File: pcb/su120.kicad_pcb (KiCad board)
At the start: 2 copper layers, 99.2 x 99.2 mm, 324 parts, among them J1 MJ-4PP-9, J2 Conn_01x03, J3 Conn_01x08, J4 Conn_01x08, J5 Conn_01x03, J6 MJ-4PP-9, SW1 SW_Push, SW10 SW_Push, SW11 SW_Push, SW12 SW_Push, SW13 SW_Push, SW14 SW_Push, SW15 SW_Push, SW16 SW_Push, SW17 SW_Push, SW18 SW_Push, SW19 SW_Push, SW2 SW_Push, SW20 SW_Push, SW3 SW_Push, SW4 SW_Push, SW5 SW_Push, SW6 SW_Push, SW7 SW_Push, SW8 SW_Push, SW9 SW_Push, U1 ProMicro

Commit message: Rev.3
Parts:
- removed the ? at (39.7, 69.1)
- removed the ? at (39.7, 59.4)
- removed the ? at (39.7, 73.8)
- removed the ? at (39.7, 64.7)
- removed the ? at (39.7, 93.5)
- removed the ? at (39.7, 98.8)
- removed the ? at (39.7, 109.9)
- removed the ? at (39.7, 114.5)
- removed the ? at (39.7, 103.2)
- removed the ? at (39.7, 119.9)
- removed the ? at (39.3, 145.7)
- removed the ? at (134.9, 59.5)
- removed the ? at (115.9, 59.5)
- removed the ? at (58.7, 78.6)
- removed the ? at (77.8, 78.6)
- removed the ? at (96.8, 78.6)
- removed the ? at (115.9, 78.6)
- removed the ? at (134.9, 78.6)
- removed the ? at (134.9, 97.6)
- removed the ? at (115.9, 97.6)
- removed the ? at (96.8, 97.6)
- removed the ? at (39.3, 150.4)
- removed the ? at (77.8, 97.6)
- removed the ? at (58.7, 97.6)
- removed the ? at (58.7, 116.7)
- removed the ? at (77.8, 116.7)
- removed the ? at (96.8, 116.7)
- removed the ? at (115.9, 116.7)
- removed the ? at (134.9, 116.7)
- removed the ? at (118.3, 135.7)
- removed the ? at (70.6, 135.7)
- removed the ? at (39.3, 134.9)
- removed the ? at (80.2, 54.8)
- removed the ? at (84.9, 54.8)
- removed the ? at (89.7, 54.8)
- removed the ? at (49.2, 54.8)
- removed the ? at (44.5, 54.8)
- removed the ? at (75.5, 54.8)
- removed the ? at (68.8, 54.8)
- removed the ? at (53.7, 54.8)
- removed the ? at (64.4, 54.8)
- removed the ? at (39.3, 141.7)
- removed the ? at (94.1, 54.8)
- removed the ? at (104.8, 54.8)
- removed the ? at (115.9, 54.8)
- removed the ? at (125.8, 54.8)
- removed the ? at (120.5, 54.8)
- removed the ? at (130.2, 54.8)
- removed the ? at (134.9, 54.8)
- removed the ? at (109.2, 54.8)
- removed the ? at (39.7, 54.8)
- removed the ? at (39.7, 78.3)
- removed the ? at (42.9, 136.4)
- removed the ? at (39.7, 88.9)
- removed the ? at (39.7, 124.2)
- removed the ? at (39.7, 131.0)
- removed the ? at (42.9, 150.4)
- removed the ? at (42.9, 141.7)
- removed the ? at (42.9, 145.7)
- removed the ? at (111.1, 142.9)
- removed H100, H101, H102, H103, H104, H105, H106, H107, H108, H109, H110, H111, H112, H141, H142, H143, H144, H145, H146, H147, H148, H149, H150, H151, H152, H49, H50, H51, H52, H53, H54, H55, H56, H57, H58, H59, H60, H61, H62, H63, H64, H65, H66, H67, H68, H69, H70, H71, H72, H73, H74, H75, H76, H77, H78, H79, H80, H81, H82, H83, H84, H85, H86, H87, H88, H89, H90, H91, H92, H93, H94, H95, H96, H97, H98, H99: MountingHole_Pad, #footprint:M2_Pad
- removed H153, H154, H155, H156, H158, H159, H160, H161, H162, H163, H164, H165, H166, H167, H168, H169, H170, H171, H172, H173, H174, H175, H176, H177, H178, H179, H180, H181, H182, H183, H184, H185, H186, H187, H188, H189, H190, H191, H192, H193, H194, H195, H196, H197, H198, H199, H200, H201, H202, H203, H204, H205, H206, H207, H208, H209: MountingHole_Pad, #footprint:M1.4_tapping_Pad
- added ?: , #footprint:M2, F.Cu at (99.2, 78.6)
- added ?: , #footprint:M1.4_tapping_Pad, F.Cu at (39.3, 142.1)
- added ?: , #footprint:M1.4_tapping_Pad, F.Cu at (39.3, 134.9)
- added ?: , #footprint:M1.4_tapping_Pad, F.Cu at (70.1, 55.2)
- added ?: , #footprint:M1.4_tapping_Pad, F.Cu at (82.9, 55.2)
- added ?: , #footprint:M1.4_tapping_Pad, F.Cu at (74.4, 55.2)
- added ?: , #footprint:M1.4_tapping_Pad, F.Cu at (40.1, 58.5)
- added ?: , #footprint:M1.4_tapping_Pad, F.Cu at (40.1, 67.1)
- added ?: , #footprint:M1.4_tapping_Pad, F.Cu at (44.5, 59.5)
- added ?: , #footprint:M1.4_tapping_Pad, F.Cu at (96.8, 59.5)
- added ?: , #footprint:M1.4_tapping_Pad, F.Cu at (101.6, 59.5)
- added ?: , #footprint:M2, F.Cu at (118.3, 73.8)
- added ?: , #footprint:M1.4_tapping_Pad, F.Cu at (115.9, 59.5)
- added ?: , #footprint:M1.4_tapping_Pad, F.Cu at (120.7, 59.5)
- added ?: , #footprint:M1.4_tapping_Pad, F.Cu at (134.9, 59.5)
- added ?: , #footprint:M1.4_tapping_Pad, F.Cu at (134.9, 73.8)
- added ?: , #footprint:M1.4_tapping_Pad, F.Cu at (120.7, 73.8)
- added ?: , #footprint:M1.4_tapping_Pad, F.Cu at (115.9, 73.8)
- added ?: , #footprint:M1.4_tapping_Pad, F.Cu at (101.6, 73.8)
- added ?: , #footprint:M1.4_tapping_Pad, F.Cu at (96.8, 73.8)
- added ?: , #footprint:M1.4_tapping_Pad, F.Cu at (44.5, 73.8)
- added ?: , #footprint:M1.4_tapping_Pad, F.Cu at (44.5, 78.6)
- added ?: , #footprint:M2, F.Cu at (115.9, 76.2)
- added ?: , #footprint:M1.4_tapping_Pad, F.Cu at (58.7, 78.6)
- added ?: , #footprint:M1.4_tapping_Pad, F.Cu at (63.5, 78.6)
- added ?: , #footprint:M1.4_tapping_Pad, F.Cu at (77.8, 78.6)
- added ?: , #footprint:M1.4_tapping_Pad, F.Cu at (82.5, 78.6)
- added ?: , #footprint:M1.4_tapping_Pad, F.Cu at (96.8, 78.6)
- added ?: , #footprint:M1.4_tapping_Pad, F.Cu at (101.6, 78.6)
- added ?: , #footprint:M1.4_tapping_Pad, F.Cu at (115.9, 78.6)
- added ?: , #footprint:M1.4_tapping_Pad, F.Cu at (120.7, 78.6)
- added ?: , #footprint:M1.4_tapping_Pad, F.Cu at (134.9, 78.6)
- added ?: , #footprint:M1.4_tapping_Pad, F.Cu at (134.9, 92.9)
- added ?: , #footprint:M2, F.Cu at (118.3, 78.6)
- added ?: , #footprint:M1.4_tapping_Pad, F.Cu at (120.7, 92.9)
- added ?: , #footprint:M1.4_tapping_Pad, F.Cu at (115.9, 92.9)
- added ?: , #footprint:M1.4_tapping_Pad, F.Cu at (101.6, 92.9)
- added ?: , #footprint:M1.4_tapping_Pad, F.Cu at (96.8, 92.9)
- added ?: , #footprint:M1.4_tapping_Pad, F.Cu at (82.5, 92.9)
- added ?: , #footprint:M1.4_tapping_Pad, F.Cu at (77.8, 92.9)
- added ?: , #footprint:M1.4_tapping_Pad, F.Cu at (63.5, 92.9)
- added ?: , #footprint:M1.4_tapping_Pad, F.Cu at (58.7, 92.9)
- added ?: , #footprint:M1.4_tapping_Pad, F.Cu at (44.5, 92.9)
- added ?: , #footprint:M1.4_tapping_Pad, F.Cu at (44.5, 97.6)
- added ?: , #footprint:M2, F.Cu at (120.7, 76.2)
- added ?: , #footprint:M1.4_tapping_Pad, F.Cu at (58.7, 97.6)
- added ?: , #footprint:M1.4_tapping_Pad, F.Cu at (63.5, 97.6)
- added ?: , #footprint:M1.4_tapping_Pad, F.Cu at (77.8, 97.6)
- added ?: , #footprint:M1.4_tapping_Pad, F.Cu at (82.5, 97.6)
- added ?: , #footprint:M1.4_tapping_Pad, F.Cu at (96.8, 97.6)
- added ?: , #footprint:M1.4_tapping_Pad, F.Cu at (101.6, 97.6)
- added ?: , #footprint:M1.4_tapping_Pad, F.Cu at (115.9, 97.6)
- added ?: , #footprint:M1.4_tapping_Pad, F.Cu at (120.7, 97.6)
- added ?: , #footprint:M1.4_tapping_Pad, F.Cu at (134.9, 97.6)
- added ?: , #footprint:M1.4_tapping_Pad, F.Cu at (134.9, 111.9)
- added ?: , #footprint:M2, F.Cu at (134.9, 76.2)
- added ?: , #footprint:M1.4_tapping_Pad, F.Cu at (120.7, 111.9)
- added ?: , #footprint:M1.4_tapping_Pad, F.Cu at (115.9, 111.9)
- added ?: , #footprint:M1.4_tapping_Pad, F.Cu at (101.6, 111.9)
- added ?: , #footprint:M1.4_tapping_Pad, F.Cu at (96.8, 111.9)
- added ?: , #footprint:M1.4_tapping_Pad, F.Cu at (82.5, 111.9)
- added ?: , #footprint:M1.4_tapping_Pad, F.Cu at (77.8, 111.9)
- added ?: , #footprint:M1.4_tapping_Pad, F.Cu at (63.5, 111.9)
- added ?: , #footprint:M1.4_tapping_Pad, F.Cu at (58.7, 111.9)
- added ?: , #footprint:M1.4_tapping_Pad, F.Cu at (44.5, 111.9)
- added ?: , #footprint:M1.4_tapping_Pad, F.Cu at (44.5, 116.7)
- added ?: , #footprint:M2, F.Cu at (134.9, 95.2)
- added ?: , #footprint:M1.4_tapping_Pad, F.Cu at (58.7, 116.7)
- added ?: , #footprint:M1.4_tapping_Pad, F.Cu at (63.5, 116.7)
- added ?: , #footprint:M1.4_tapping_Pad, F.Cu at (77.8, 116.7)
- added ?: , #footprint:M1.4_tapping_Pad, F.Cu at (82.5, 116.7)
- added ?: , #footprint:M1.4_tapping_Pad, F.Cu at (96.8, 116.7)
- added ?: , #footprint:M1.4_tapping_Pad, F.Cu at (101.6, 116.7)
- added ?: , #footprint:M1.4_tapping_Pad, F.Cu at (115.9, 116.7)
- added ?: , #footprint:M1.4_tapping_Pad, F.Cu at (120.7, 116.7)
- added ?: , #footprint:M1.4_tapping_Pad, F.Cu at (134.9, 116.7)
- added ?: , #footprint:M1.4_tapping_Pad, F.Cu at (134.9, 131.0)
- added ?: , #footprint:M2, F.Cu at (118.3, 92.9)
- added ?: , #footprint:M1.4_tapping_Pad, F.Cu at (120.7, 131.0)
- added ?: , #footprint:M1.4_tapping_Pad, F.Cu at (115.9, 131.0)
- added ?: , #footprint:M1.4_tapping_Pad, F.Cu at (101.6, 131.0)
- added ?: , #footprint:M1.4_tapping_Pad, F.Cu at (96.8, 131.0)
- added ?: , #footprint:M1.4_tapping_Pad, F.Cu at (82.5, 131.0)
- added ?: , #footprint:M1.4_tapping_Pad, F.Cu at (77.8, 131.0)
- added ?: , #footprint:M1.4_tapping_Pad, F.Cu at (63.5, 131.0)
- added ?: , #footprint:M1.4_tapping_Pad, F.Cu at (58.7, 131.0)
- added ?: , #footprint:M1.4_tapping_Pad, F.Cu at (44.5, 131.0)
- added ?: , #footprint:M1.4_tapping_Pad, F.Cu at (63.5, 135.7)
- added ?: , #footprint:M2, F.Cu at (120.7, 95.2)
- added ?: , #footprint:M1.4_tapping_Pad, F.Cu at (73.0, 135.7)
- added ?: , #footprint:M1.4_tapping_Pad, F.Cu at (87.3, 135.7)
- added ?: , #footprint:M1.4_tapping_Pad, F.Cu at (96.8, 135.7)
- added ?: , #footprint:M1.4_tapping_Pad, F.Cu at (101.6, 135.7)
- added ?: , #footprint:M1.4_tapping_Pad, F.Cu at (115.9, 135.7)
- added ?: , #footprint:M1.4_tapping_Pad, F.Cu at (120.7, 135.7)
- added ?: , #footprint:M1.4_tapping_Pad, F.Cu at (134.9, 135.7)
- added ?: , #footprint:M1.4_tapping_Pad, F.Cu at (134.9, 150.0)
- added ?: , #footprint:M1.4_tapping_Pad, F.Cu at (120.7, 150.0)
- added ?: , #footprint:M1.4_tapping_Pad, F.Cu at (115.9, 150.0)
- added ?: , #footprint:M2, F.Cu at (118.3, 97.6)
- added ?: , #footprint:M1.4_tapping_Pad, F.Cu at (101.6, 150.0)
- added ?: , #footprint:M1.4_tapping_Pad, F.Cu at (96.8, 150.0)
- added ?: , #footprint:M1.4_tapping_Pad, F.Cu at (87.3, 150.0)
- added ?: , #footprint:M1.4_tapping_Pad, F.Cu at (73.0, 150.0)
- added ?: , #footprint:M1.4_tapping_Pad, F.Cu at (63.5, 150.0)
- added ?: , #footprint:M1.4_tapping_Pad, F.Cu at (43.3, 142.1)
- added ?: , #footprint:M1.4_tapping_Pad, F.Cu at (43.3, 135.3)
- added ?: , #footprint:M1.4_tapping_Pad, F.Cu at (130.0, 55.2)
- added ?: , #footprint:M1.4_tapping_Pad, F.Cu at (135.3, 55.2)
- added ?: , #footprint:M1.4_tapping_Pad, F.Cu at (91.7, 55.2)
- added ?: , #footprint:M2, F.Cu at (134.9, 133.3)
- added ?: , #footprint:M2, F.Cu at (115.9, 95.2)
- added ?: , #footprint:M1.4_tapping_Pad, F.Cu at (86.4, 55.2)
- added ?: , #footprint:M1.4_tapping_Pad, F.Cu at (121.3, 55.2)
- added ?: , #footprint:M1.4_tapping_Pad, F.Cu at (112.5, 55.2)
- added ?: , #footprint:M1.4_tapping_Pad, F.Cu at (117.9, 55.2)
- added ?: , #footprint:M1.4_tapping_Pad, F.Cu at (126.6, 55.2)
- added ?: , #footprint:M1.4_tapping_Pad, F.Cu at (95.1, 55.2)
- added ?: , #footprint:M1.4_tapping_Pad, F.Cu at (100.4, 55.2)
- added ?: , #footprint:M1.4_tapping_Pad, F.Cu at (109.1, 55.2)
- added ?: , #footprint:M1.4_tapping_Pad, F.Cu at (103.8, 55.2)
- added ?: , #footprint:M1.4_tapping_Pad, F.Cu at (43.3, 150.4)
- added ?: , #footprint:M2, F.Cu at (99.2, 92.9)
- added ?: , #footprint:M1.4_tapping_Pad, F.Cu at (43.3, 145.7)
- added ?: , #footprint:M2, F.Cu at (101.6, 95.2)
- added ?: , #footprint:M2, F.Cu at (99.2, 97.6)
- added ?: , #footprint:M2, F.Cu at (96.8, 95.2)
- added ?: , #footprint:M2, F.Cu at (80.2, 92.9)
- added ?: , #footprint:M2, F.Cu at (82.5, 95.2)
- added ?: , #footprint:M2, F.Cu at (80.2, 97.6)
- added ?: , #footprint:M2, F.Cu at (77.8, 95.2)
- added ?: , #footprint:M2, F.Cu at (61.1, 92.9)
- added ?: , #footprint:M2, F.Cu at (80.2, 59.5)
- added ?: , #footprint:M2, F.Cu at (63.5, 95.2)
- added ?: , #footprint:M2, F.Cu at (61.1, 97.6)
- added ?: , #footprint:M2, F.Cu at (58.7, 95.2)
- added ?: , #footprint:M2, F.Cu at (44.5, 95.2)
- added ?: , #footprint:M2, F.Cu at (44.5, 114.3)
- added ?: , #footprint:M2, F.Cu at (58.7, 114.3)
- added ?: , #footprint:M2, F.Cu at (61.1, 111.9)
- added ?: , #footprint:M2, F.Cu at (63.5, 114.3)
- added ?: , #footprint:M2, F.Cu at (61.1, 116.7)
- added ?: , #footprint:M2, F.Cu at (77.8, 114.3)
- added ?: , #footprint:M2, F.Cu at (80.2, 73.8)
- added ?: , #footprint:M2, F.Cu at (80.2, 111.9)
- added ?: , #footprint:M2, F.Cu at (82.5, 114.3)
- added ?: , #footprint:M2, F.Cu at (80.2, 116.7)
- added ?: , #footprint:M2, F.Cu at (96.8, 114.3)
- added ?: , #footprint:M2, F.Cu at (99.2, 111.9)
- added ?: , #footprint:M2, F.Cu at (101.6, 114.3)
- added ?: , #footprint:M2, F.Cu at (99.2, 116.7)
- added ?: , #footprint:M2, F.Cu at (115.9, 114.3)
- added ?: , #footprint:M2, F.Cu at (118.3, 111.9)
- added ?: , #footprint:M2, F.Cu at (120.7, 114.3)
- added ?: , #footprint:M2, F.Cu at (115.9, 133.3)
- added ?: , #footprint:M2, F.Cu at (118.3, 116.7)
- added ?: , #footprint:M2, F.Cu at (134.9, 114.3)
- added ?: , #footprint:M2, F.Cu at (118.3, 150.0)
- added ?: , #footprint:M2, F.Cu at (120.7, 133.3)
- added ?: , #footprint:M2, F.Cu at (118.3, 135.7)
- added ?: , #footprint:M2, F.Cu at (118.3, 131.0)
- added ?: , #footprint:M2, F.Cu at (101.6, 133.3)
- added ?: , #footprint:M2, F.Cu at (96.8, 133.3)
- added ?: , #footprint:M2, F.Cu at (99.2, 150.0)
- added ?: , #footprint:M2, F.Cu at (99.2, 135.7)
- added ?: , #footprint:M2, F.Cu at (118.3, 59.5)
- added ?: , #footprint:M2, F.Cu at (99.2, 131.0)
- added ?: , #footprint:M2, F.Cu at (80.2, 131.0)
- added ?: , #footprint:M2, F.Cu at (61.1, 131.0)
- added ?: , #footprint:M1.4_tapping_Pad, F.Cu at (42.9, 55.2)
- added ?: , #footprint:M1.4_tapping_Pad, F.Cu at (52.4, 55.2)
- added ?: , #footprint:M1.4_tapping_Pad, F.Cu at (47.6, 55.2)
- added ?: , #footprint:M1.4_tapping_Pad, F.Cu at (59.1, 141.8)
- added ?: , #footprint:M1.4_tapping_Pad, F.Cu at (39.3, 145.7)
- added ?: , #footprint:M1.4_tapping_Pad, F.Cu at (39.3, 150.4)
- added ?: , #footprint:M1.4_tapping_Pad, F.Cu at (47.2, 150.4)
- added ?: , #footprint:M2, F.Cu at (61.1, 78.6)
- added ?: , #footprint:M1.4_tapping_Pad, F.Cu at (47.2, 142.1)
- added ?: , #footprint:M1.4_tapping_Pad, F.Cu at (47.2, 145.7)
- added ?: , #footprint:M1.4_tapping_Pad, F.Cu at (47.2, 135.3)
- added ?: , #footprint:M1.4_tapping_Pad, F.Cu at (51.2, 142.1)
- added ?: , #footprint:M1.4_tapping_Pad, F.Cu at (51.2, 145.7)
- added ?: , #footprint:M1.4_tapping_Pad, F.Cu at (51.2, 135.3)
- added ?: , #footprint:M1.4_tapping_Pad, F.Cu at (51.2, 150.4)
- added ?: , #footprint:M1.4_tapping_Pad, F.Cu at (55.2, 142.1)
- added ?: , #footprint:M1.4_tapping_Pad, F.Cu at (55.2, 145.7)
- added ?: , #footprint:M1.4_tapping_Pad, F.Cu at (55.2, 135.3)
- added ?: , #footprint:M2, F.Cu at (80.2, 78.6)
- added ?: , #footprint:M1.4_tapping_Pad, F.Cu at (55.2, 150.4)
- added ?: , #footprint:M1.4_tapping_Pad, F.Cu at (59.1, 135.4)
- added ?: , #footprint:M1.4_tapping_Pad, F.Cu at (59.1, 150.4)
- added ?: , #footprint:M1.4_tapping_Pad, F.Cu at (40.1, 80.2)
- added ?: , #footprint:M1.4_tapping_Pad, F.Cu at (40.1, 75.4)
- added ?: , #footprint:M1.4_tapping_Pad, F.Cu at (40.1, 84.9)
- added ?: , #footprint:M1.4_tapping_Pad, F.Cu at (40.1, 70.6)
- added ?: , #footprint:M1.4_tapping_Pad, F.Cu at (40.1, 88.5)
- added ?: , #footprint:M1.4_tapping_Pad, F.Cu at (40.1, 98.0)
- added ?: , #footprint:M1.4_tapping_Pad, F.Cu at (40.1, 102.8)
- added ?: , #footprint:M2, F.Cu at (101.6, 76.2)
- added ?: , #footprint:M1.4_tapping_Pad, F.Cu at (40.1, 93.3)
- added ?: , #footprint:M1.4_tapping_Pad, F.Cu at (56.0, 55.2)
- added ?: , #footprint:M1.4_tapping_Pad, F.Cu at (59.9, 55.2)
- added ?: , #footprint:M1.4_tapping_Pad, F.Cu at (66.7, 55.2)
- added ?: , #footprint:M1.4_tapping_Pad, F.Cu at (40.1, 106.4)
- added ?: , #footprint:M1.4_tapping_Pad, F.Cu at (40.1, 111.1)
- added ?: , #footprint:M1.4_tapping_Pad, F.Cu at (40.1, 120.7)
- added ?: , #footprint:M1.4_tapping_Pad, F.Cu at (40.1, 115.9)
- added ?: , #footprint:M1.4_tapping_Pad, F.Cu at (40.1, 131.4)
- added ?: , #footprint:M1.4_tapping_Pad, F.Cu at (40.1, 124.2)
- added D20: D, #footprint:diode_TH_SMD, F.Cu at (125.8, 134.9)
- added H210: MountingHole_Pad, #footprint:1pin_conn, F.Cu at (123.4, 134.9)
- added H211: MountingHole_Pad, #footprint:1pin_conn, F.Cu at (123.4, 150.8)
- added H212: MountingHole_Pad, #footprint:1pin_conn, F.Cu at (119.9, 143.3)
- added H213: MountingHole_Pad, #footprint:1pin_conn, F.Cu at (135.7, 143.3)
- added SW21: SW_Push, #footprint:CherryMX_MidHeight_Choc_Hotswap_rev4, F.Cu at (127.8, 142.9)
- SW1, SW10, SW11, SW12, SW13, SW14, SW15, SW16, SW17, SW19, SW2, SW20, SW3, SW4, SW5, SW6, SW7, SW8, SW9: footprint #footprint:CherryMX_MidHeight_Choc_Hotswap_rev2 -> #footprint:CherryMX_MidHeight_Choc_Hotswap_rev4
- moved ? 16.7 mm to (80.2, 142.9)
- moved D16 16.7 mm to (78.2, 134.9)
- moved H45 16.7 mm to (72.2, 143.3)
- moved H46 16.7 mm to (88.1, 143.3)
- moved SW16 16.7 mm to (80.2, 142.9)
- moved H41 16.7 mm to (75.8, 134.9)
- moved H43 16.7 mm to (75.8, 150.8)
- moved H42 2.38 mm to (104.4, 134.9)
- moved H44 2.38 mm to (104.4, 150.8)
- moved D17 2.38 mm to (106.8, 134.9)
- moved H47 2.38 mm to (100.8, 143.3)
- moved H48 2.38 mm to (116.7, 143.3)
- moved SW17 2.38 mm to (108.7, 142.9)
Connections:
- H41 pad 1: X1 -> X2
- H43 pad 1: X1 -> X2
- J1 pad A: Net-(J1-PadA) -> (no net)
- J6 pad A: Net-(J6-PadA) -> (no net)
- SW16 pad 1: X1 -> X2
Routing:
- net GND: track 1208.9 -> 978.4 mm, vias 52 -> 115
- net X2: track 87.2 -> 120.6 mm
- net X1: track 127.4 -> 95.9 mm
- net X5: track 153.9 -> 180.2 mm
- net Y5: track 252.8 -> 277.5 mm
- net Net-(D20-Pad2): track 0.00 -> 18.2 mm
- net X3: track 99.7 -> 101.5 mm
- net (no net): track 0.00 -> 1.68 mm
- net X4: track 160.0 -> 161.5 mm
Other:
- board size 99.2 x 99.2 mm -> 99.2 x 98.4 mm
- board text added: "0.25u"
- board text added: "0.5u"
- board text added: "0.75u"
- board text added: "1.25u"
- board text added: "1.5u"
- board text added: "1/8u"
- board text added: "1u"
- board text added: "2u"
- board text added: "3/8u"
- board text added: "5/8u"
- board text added: "SU120 Rev.3 by @e3w2q"
- board text added: "stagger"
- board text removed: "1/2"
- board text removed: "1/4"
- board text removed: "1/8"
- board text removed: "SU120 Rev.2 by @e3w2q"

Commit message: update
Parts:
- removed the ? at (99.2, 78.6)
- removed the ? at (118.3, 73.8)
- removed the ? at (115.9, 76.2)
- removed the ? at (118.3, 78.6)
- removed the ? at (120.7, 76.2)
- removed the ? at (134.9, 76.2)
- removed the ? at (134.9, 95.2)
- removed the ? at (118.3, 92.9)
- removed the ? at (120.7, 95.2)
- removed the ? at (118.3, 97.6)
- removed the ? at (134.9, 133.3)
- removed the ? at (115.9, 95.2)
- removed the ? at (99.2, 92.9)
- removed the ? at (101.6, 95.2)
- removed the ? at (99.2, 97.6)
- removed the ? at (96.8, 95.2)
- removed the ? at (80.2, 92.9)
- removed the ? at (82.5, 95.2)
- removed the ? at (80.2, 97.6)
- removed the ? at (77.8, 95.2)
- removed the ? at (61.1, 92.9)
- removed the ? at (63.5, 95.2)
- removed the ? at (61.1, 97.6)
- removed the ? at (58.7, 95.2)
- removed the ? at (44.5, 95.2)
- removed the ? at (44.5, 114.3)
- removed the ? at (58.7, 114.3)
- removed the ? at (61.1, 111.9)
- removed the ? at (63.5, 114.3)
- removed the ? at (61.1, 116.7)
- removed the ? at (77.8, 114.3)
- removed the ? at (80.2, 111.9)
- removed the ? at (82.5, 114.3)
- removed the ? at (80.2, 116.7)
- removed the ? at (96.8, 114.3)
- removed the ? at (99.2, 111.9)
- removed the ? at (101.6, 114.3)
- removed the ? at (99.2, 116.7)
- removed the ? at (115.9, 114.3)
- removed the ? at (118.3, 111.9)
- removed the ? at (120.7, 114.3)
- removed the ? at (115.9, 133.3)
- removed the ? at (118.3, 116.7)
- removed the ? at (134.9, 114.3)
- removed the ? at (118.3, 150.0)
- removed the ? at (120.7, 133.3)
- removed the ? at (118.3, 135.7)
- removed the ? at (118.3, 131.0)
- removed the ? at (101.6, 133.3)
- removed the ? at (96.8, 133.3)
- removed the ? at (99.2, 150.0)
- removed the ? at (99.2, 135.7)
- removed the ? at (118.3, 59.5)
- removed the ? at (99.2, 131.0)
- removed the ? at (80.2, 131.0)
- removed the ? at (61.1, 131.0)
- removed the ? at (61.1, 78.6)
- removed the ? at (80.2, 78.6)
- removed the ? at (101.6, 76.2)
- added ?: , #footprint:M2_spacer, F.Cu at (118.3, 76.2)
- added ?: , #footprint:M2_spacer, F.Cu at (118.3, 133.3)
- added ?: , #footprint:M2_spacer, F.Cu at (99.2, 133.3)
- added ?: , #footprint:M2_spacer, F.Cu at (118.3, 95.2)
- added ?: , #footprint:M2_spacer, F.Cu at (99.2, 95.2)
- added ?: , #footprint:M2_spacer, F.Cu at (80.2, 95.2)
- added ?: , #footprint:M2_spacer, F.Cu at (61.1, 95.2)
- added ?: , #footprint:M2_spacer, F.Cu at (61.1, 114.3)
- added ?: , #footprint:M2_spacer, F.Cu at (80.2, 114.3)
- added ?: , #footprint:M2_spacer, F.Cu at (99.2, 114.3)
- added ?: , #footprint:M2_spacer, F.Cu at (118.3, 114.3)
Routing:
- net (no net): track 1.68 -> 0.00 mm
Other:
- outline, holes or cut-outs redrawn

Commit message: Rev.4
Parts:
- removed the ? at (118.3, 133.3)
- removed the ? at (99.2, 133.3)
- removed the ? at (118.3, 95.2)
- removed the ? at (99.2, 95.2)
- removed the ? at (80.2, 95.2)
- removed the ? at (61.1, 95.2)
- removed the ? at (61.1, 114.3)
- removed the ? at (80.2, 114.3)
- removed the ? at (99.2, 114.3)
- removed the ? at (118.3, 114.3)
- removed H157: MountingHole_Pad, #footprint:M1.4_tapping_Pad
- added ?: , #footprint:M2_spacer, F.Cu at (99.2, 133.4)
- added ?: , #footprint:M2_spacer, F.Cu at (118.3, 95.3)
- added ?: , #footprint:M2_spacer, F.Cu at (118.3, 133.4)
- added ?: , #footprint:M2_spacer, F.Cu at (118.3, 114.3)
- added ?: , #footprint:M2_spacer, F.Cu at (99.2, 114.3)
- added ?: , #footprint:M2_spacer, F.Cu at (80.2, 114.3)
- added ?: , #footprint:M2_spacer, F.Cu at (61.1, 114.3)
- added ?: , #footprint:M2_spacer, F.Cu at (61.1, 95.3)
- added ?: , #footprint:M2_spacer, F.Cu at (80.2, 95.3)
- added ?: , #footprint:M2_spacer, F.Cu at (99.2, 95.3)
- J3, J4: footprint #footprint:PinHeader_1x08_P2.54mm_Vertical -> #footprint:PinHeader_1x08_P2.54mm_Vertical_rev2
- JP1, JP4, JP6: moved to F.Cu
- JP2, JP3, JP5: moved to B.Cu
- moved SW18 2.31 mm to (83.7, 64.4)
- moved JP2 1.26 mm to (46.8, 69.1)
- moved JP6 1.26 mm to (46.8, 69.1)
- moved JP1 1.26 mm to (46.8, 64.3)
- moved JP3 1.26 mm to (46.8, 64.3)
- moved JP4 1.19 mm to (46.8, 66.7)
- moved JP5 1.19 mm to (46.8, 66.7)
- moved J2 0.44 mm to (88.0, 72.0)
- moved J5 0.44 mm to (93.1, 72.0)
- moved ? 0.40 mm to (39.3, 142.5)
- moved ? 0.40 mm to (39.3, 135.3)
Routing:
- net GND: track 978.4 -> 988.5 mm, vias 115 -> 117
- net reset1: track 59.2 -> 55.2 mm, vias 5 -> 3
- net Y3: track 262.4 -> 264.7 mm
- net Y4: track 307.3 -> 309.6 mm
- net dummyVCC: track 53.4 -> 55.7 mm, vias 2 -> 1
- net X4: track 161.5 -> 163.1 mm
- net dummydata: track 53.2 -> 54.4 mm, vias 2 -> 1
- net reset2: track 41.3 -> 40.1 mm, vias 2 -> 1
- net X3: track 101.5 -> 102.2 mm
- net data: track 55.8 -> 55.1 mm, vias 1 -> 2
- net Y1: track 137.2 -> 136.7 mm
- net X5: track 180.2 -> 180.5 mm, vias 1 -> 2
- net VCC: track 66.3 -> 66.1 mm, vias 2 -> 3
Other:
- board size 99.2 x 98.4 mm -> 98.8 x 98 mm
- board text added: "LED Tape"
- board text added: "SU120 Rev.4 by @e3w2q"
- board text added: "See back side printing for pin mapping"
- board text added: "Solder back side jumper"
- board text added: "back side only"
- board text removed: "SU120 Rev.3 by @e3w2q"
- board text removed: "See back side printing for pin numbers"
- board text removed: "Solder front side jumper"

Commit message: fix PCB
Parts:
- ?: footprint #footprint:CherryMX_MidHeight_Choc_Hotswap_2U_Outline -> #footprint:CherryMX_Choc_Hotswap_2U_Outline
- ?: footprint #footprint:M1.4_tapping_Pad -> #footprint:M1.4_tapping_Pad_1.8mm
- SW1, SW10, SW11, SW12, SW13, SW14, SW15, SW16, SW17, SW19, SW2, SW20, SW21, SW3, SW4, SW5, SW6, SW7, SW8, SW9: footprint #footprint:CherryMX_MidHeight_Choc_Hotswap_rev4 -> #footprint:CherryMX_Choc_Hotswap_rev4
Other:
- outline, holes or cut-outs redrawn

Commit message: rev5
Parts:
- added H49: MountingHole_Pad, #footprint:1pin_conn, F.Cu at (62.7, 143.3)
- added H50: MountingHole_Pad, #footprint:1pin_conn, F.Cu at (97.6, 143.3)
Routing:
- net Y5: track 278.0 -> 302.6 mm
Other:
- outline, holes or cut-outs redrawn

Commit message: Rev6
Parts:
- added ?: , #footprint:CherryMX_MidHeight_Choc_Silk_Line, F.Cu at (90.5, 143.3)
- added ?: , #footprint:CherryMX_MidHeight_Choc_Silk, F.Cu at (127.8, 142.9)
- added ?: , #footprint:CherryMX_MidHeight_Choc_Silk, F.Cu at (108.7, 142.9)
- added ?: , #footprint:CherryMX_MidHeight_Choc_Silk, F.Cu at (80.2, 142.9)
- added ?: , #footprint:CherryMX_MidHeight_Choc_Silk, F.Cu at (51.6, 123.8)
- added ?: , #footprint:CherryMX_MidHeight_Choc_Silk, F.Cu at (70.6, 123.8)
- added ?: , #footprint:CherryMX_MidHeight_Choc_Silk, F.Cu at (89.7, 123.8)
- added ?: , #footprint:CherryMX_MidHeight_Choc_Silk, F.Cu at (108.7, 123.8)
- added ?: , #footprint:CherryMX_MidHeight_Choc_Silk, F.Cu at (127.8, 123.8)
- added ?: , #footprint:CherryMX_MidHeight_Choc_Silk, F.Cu at (127.8, 104.8)
- added ?: , #footprint:CherryMX_MidHeight_Choc_Silk, F.Cu at (108.7, 104.8)
- added ?: , #footprint:CherryMX_MidHeight_Choc_Silk, F.Cu at (89.7, 104.8)
- added ?: , #footprint:CherryMX_MidHeight_Choc_Silk, F.Cu at (70.6, 104.8)
- added ?: , #footprint:CherryMX_MidHeight_Choc_Silk, F.Cu at (51.6, 104.8)
- added ?: , #footprint:CherryMX_MidHeight_Choc_Silk, F.Cu at (51.6, 85.7)
- added ?: , #footprint:CherryMX_MidHeight_Choc_Silk, F.Cu at (70.6, 85.7)
- added ?: , #footprint:CherryMX_MidHeight_Choc_Silk, F.Cu at (89.7, 85.7)
- added ?: , #footprint:CherryMX_MidHeight_Choc_Silk, F.Cu at (127.8, 85.7)
- added ?: , #footprint:CherryMX_MidHeight_Choc_Silk, F.Cu at (108.7, 85.7)
- added ?: , #footprint:CherryMX_MidHeight_Choc_Silk_Line, F.Cu at (70.2, 143.3)
- added ?: , #footprint:CherryMX_MidHeight_Choc_Silk_Line, F.Cu at (123.0, 66.7)
- added ?: , #footprint:CherryMX_MidHeight_Choc_Silk_Line, F.Cu at (104.0, 66.7)
- added ?: , #footprint:CherryMX_MidHeight_Choc_Silk_Line, F.Cu at (108.7, 63.5)
- added ?: , #footprint:CherryMX_MidHeight_Choc_Silk_Line, F.Cu at (127.8, 63.5)
- added ?: , #footprint:M2_Hole, F.Cu at (61.1, 152.4)
- added ?: , #footprint:M2_Hole, F.Cu at (137.3, 57.2)
- added ?: , #footprint:M2_Hole, F.Cu at (61.1, 133.3)
- added ?: , #footprint:M2_Hole, F.Cu at (99.2, 152.4)
- added ?: , #footprint:M2_Hole, F.Cu at (118.3, 152.4)
- added ?: , #footprint:M2_Hole, F.Cu at (137.3, 152.4)
- added ?: , #footprint:M2_Hole, F.Cu at (137.3, 133.3)
- added ?: , #footprint:M2_Hole, F.Cu at (137.3, 114.3)
- added ?: , #footprint:M2_Hole, F.Cu at (137.3, 95.2)
- added ?: , #footprint:M2_Hole, F.Cu at (137.3, 76.2)
- added ?: , #footprint:M2_Hole, F.Cu at (99.2, 76.2)
- added H51: MountingHole_Pad, #footprint:1pin_conn, F.Cu at (111.1, 61.5)
- added H52: MountingHole_Pad, #footprint:1pin_conn, F.Cu at (127.8, 61.5)
- added H53: MountingHole_Pad, #footprint:1pin_conn, F.Cu at (106.4, 61.5)
- added H54: MountingHole_Pad, #footprint:1pin_conn, F.Cu at (130.2, 61.5)
- added H55: MountingHole_Pad, #footprint:1pin_conn, F.Cu at (108.7, 61.5)
- added H56: MountingHole_Pad, #footprint:1pin_conn, F.Cu at (125.4, 61.5)
- ? (x147): footprint #footprint:M1.4_tapping_Pad -> #footprint:M1.4_tapping_Hole
- ? (x11): footprint #footprint:M2_spacer -> #footprint:M2_Hole
- ? (x2): footprint #footprint:M2 -> #footprint:M2_Hole
- ?: footprint #footprint:M1.4_tapping_Pad_1.8mm -> #footprint:M1.4_tapping_Hole
- SW1, SW10, SW11, SW12, SW13, SW14, SW15, SW16, SW17, SW2, SW21, SW3, SW4, SW5, SW6, SW7, SW8, SW9: footprint #footprint:CherryMX_Choc_Hotswap_rev4 -> #footprint:CherryMX_MidHeight_Choc_Hotswap_rev5
- SW19, SW20: value SW_Push -> Rotary_Encoder_Switch; footprint #footprint:CherryMX_Choc_Hotswap_rev4 -> #footprint:RotaryEncoder_Alps_EC11E-Switch_Vertical_H20mm_rev2
- U1: footprint #footprint:ArduinoProMicro-ZigZag_rev4 -> #footprint:ArduinoProMicro-ZigZag_rev5
- moved D18 12.2 mm to (116.7, 65.9), turned to 270 degrees
- moved D19 12.2 mm to (135.7, 65.9), turned to 270 degrees
- moved H137 3.57 mm to (100.8, 63.5)
- moved H138 3.57 mm to (116.7, 63.5)
- moved H139 3.57 mm to (119.9, 63.5)
- moved H140 3.57 mm to (135.7, 63.5)
- moved H136 0.40 mm to (123.0, 74.6)
- moved H135 0.40 mm to (104.0, 74.6)
- moved H133 0.40 mm to (104.0, 58.7)
- moved H134 0.40 mm to (123.0, 58.7)
- moved J2 0.20 mm to (88.0, 71.8)
- moved J5 0.20 mm to (93.1, 71.8)
- turned SW19 to 270 degrees
- turned SW20 to 270 degrees
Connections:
- D1 pad 1: Y2 -> Y1
- D10 pad 1: Y3 -> Y2
- D11 pad 1: Y4 -> Y3
- D12 pad 1: Y4 -> Y3
- D13 pad 1: Y4 -> Y3
- D14 pad 1: Y4 -> Y3
- D15 pad 1: Y4 -> Y3
- D16 pad 1: Y5 -> Y4
- D17 pad 1: Y5 -> Y4
- D18 pad 1: Y1 -> Y6
- D19 pad 1: Y1 -> Y6
- D2 pad 1: Y2 -> Y1
- D20 pad 1: Y5 -> Y4
- D3 pad 1: Y2 -> Y1
- D4 pad 1: Y2 -> Y1
- D5 pad 1: Y2 -> Y1
- D6 pad 1: Y3 -> Y2
- D7 pad 1: Y3 -> Y2
- D8 pad 1: Y3 -> Y2
- D9 pad 1: Y3 -> Y2
- H11 pad 1: Y2 -> Y1
- H12 pad 1: Y2 -> Y1
- H123 pad 1: Y4 -> Y3
- H124 pad 1: Y4 -> Y3
- H125 pad 1: Y4 -> Y3
- H126 pad 1: Y4 -> Y3
- H127 pad 1: Y4 -> Y3
- H128 pad 1: Y4 -> Y3
- H129 pad 1: Y4 -> Y3
- H13 pad 1: Y2 -> Y1
- H130 pad 1: Y4 -> Y3
- H131 pad 1: Y4 -> Y3
- H132 pad 1: Y4 -> Y3
- H137 pad 1: Y1 -> Y6
- H138 pad 1: Y1 -> Y6
- H139 pad 1: Y1 -> Y6
- H14 pad 1: Y2 -> Y1
- H140 pad 1: Y1 -> Y6
- H15 pad 1: Y2 -> Y1
- H16 pad 1: Y2 -> Y1
- H17 pad 1: Y2 -> Y1
- H18 pad 1: Y2 -> Y1
- H19 pad 1: Y2 -> Y1
- H20 pad 1: Y2 -> Y1
- H212 pad 1: Y5 -> Y4
- H213 pad 1: Y5 -> Y4
- H31 pad 1: Y3 -> Y2
- H32 pad 1: Y3 -> Y2
- H33 pad 1: Y3 -> Y2
- H34 pad 1: Y3 -> Y2
- H35 pad 1: Y3 -> Y2
- H36 pad 1: Y3 -> Y2
- H37 pad 1: Y3 -> Y2
- H38 pad 1: Y3 -> Y2
- H39 pad 1: Y3 -> Y2
- H40 pad 1: Y3 -> Y2
- H45 pad 1: Y5 -> Y4
- H46 pad 1: Y5 -> Y4
- H47 pad 1: Y5 -> Y4
- H48 pad 1: Y5 -> Y4
- H49 pad 1: Y5 -> Y4
- H50 pad 1: Y5 -> Y4
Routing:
- net Y5: track 302.6 -> 5.47 mm, vias 6 -> 0
- net Y1: track 136.7 -> 234.4 mm, vias 0 -> 2
- net X9: track 5.47 -> 95.4 mm, vias 0 -> 2
- net Y6: track 5.01 -> 92.0 mm
- net X10: track 5.04 -> 86.9 mm, vias 0 -> 2
- net X8: track 5.01 -> 52.5 mm, vias 0 -> 1
- net Y3: track 264.7 -> 312.1 mm, vias 2 -> 6
- net X7: track 5.47 -> 50.9 mm, vias 0 -> 2
- net Y2: track 236.5 -> 266.4 mm
- net X4: track 163.1 -> 184.3 mm, vias 0 -> 1
- net GND: track 988.5 -> 1009.4 mm, vias 117 -> 122
- net Net-(D18-Pad2): track 18.2 -> 8.90 mm
- net Net-(D19-Pad2): track 18.2 -> 8.90 mm
- net reset1: track 55.2 -> 52.1 mm
- net dummyVCC: track 55.7 -> 57.8 mm
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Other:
- outline, holes or cut-outs redrawn
- board text added: "LED Tape(back side)"
- board text added: "SU120 "YAKITORI" Rev.6 by @e3w2q"
- board text removed: "LED Tape"
- board text removed: "SU120 Rev.4 by @e3w2q"
- board text removed: "back side only"

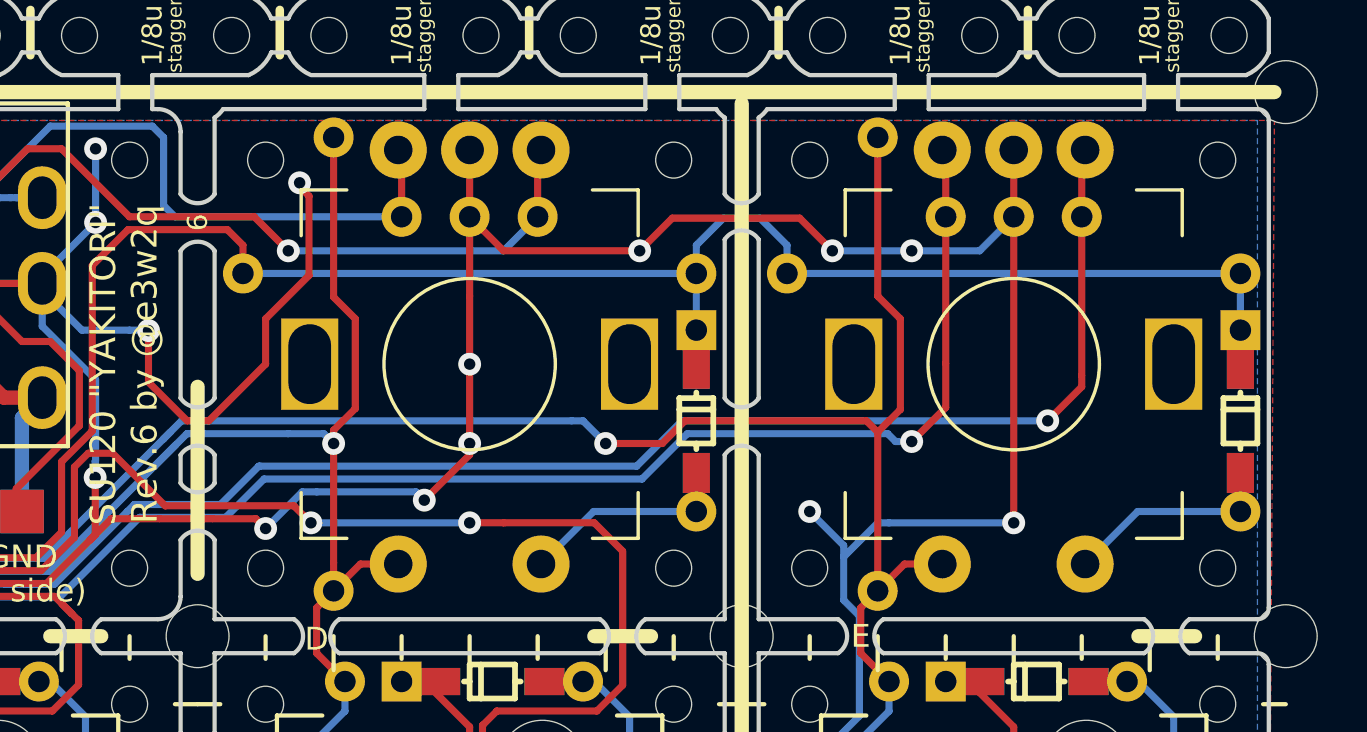
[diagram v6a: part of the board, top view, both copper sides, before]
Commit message: Rotary Encoder's pin exchanged
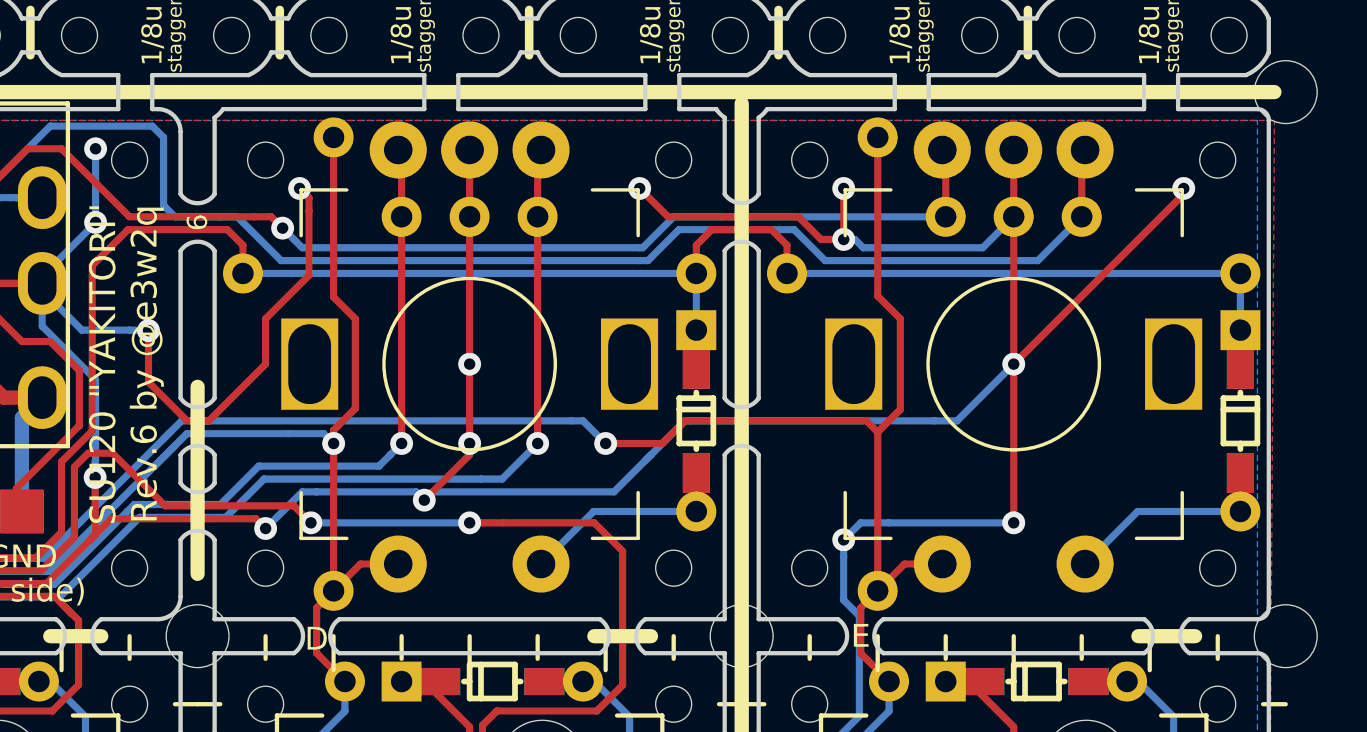
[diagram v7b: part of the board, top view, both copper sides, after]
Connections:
- H51 pad 1: X7 -> X10
- H53 pad 1: X8 -> X9
- H54 pad 1: X9 -> X8
- H56 pad 1: X10 -> X7
- SW19 pad A: X7 -> X10
- SW19 pad B: X8 -> X9
- SW20 pad A: X9 -> X8
- SW20 pad B: X10 -> X7
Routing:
- net X8: track 52.5 -> 78.4 mm
- net GND: track 1009.4 -> 1034.3 mm, vias 122 -> 124
- net X9: track 95.4 -> 72.8 mm
- net X7: track 50.9 -> 65.1 mm
- net X10: track 86.9 -> 73.2 mm
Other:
- outline, holes or cut-outs redrawn
